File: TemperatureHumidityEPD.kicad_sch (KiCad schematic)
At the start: 66 parts, among them J1 Conn_01x02, J2 FTSH-105-01-L-DV-K, J3 Conn_01x08, J4 Conn_01x24, Q1 Si1308EDL, Q2 IRLML6344, SW1 SW_Push, U1 SI7021, U2 MAX32660GTP, U3 MAX20343H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

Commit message: Fix Part Number for 1k resistor
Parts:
- R6, R7: Part Number RCS06030000Z0EC -> RT0603FRE131KL
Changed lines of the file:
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@@
       (effects (font (size 1.27 1.27)) hide)
     )
-    (property "Part Number" "RCS06030000Z0EC" (at 117.475 184.15 0)
-      (effects (font (size 1.27 1.27)) hide)
-    )
-    (property "Description" "resistor, 0, 0.25W, thick film, SMT, 0603 (1608)" (at 117.475 184.15 0)
+    (property "Part Number" "RT0603FRE131KL" (at 117.475 184.15 0)
+      (effects (font (size 1.27 1.27)) hide)
+    )
+    (property "Description" "resistor, 1k, 0.1W, thin film, 1%, 50ppm, SMT, 0603 (1608)" (at 117.475 184.15 0)
       (effects (font (size 1.27 1.27)) hide)
     )
@@
       (effects (font (size 1.27 1.27)) hide)
     )
-    (property "Part Number" "RCS06030000Z0EC" (at 117.475 179.705 0)
-      (effects (font (size 1.27 1.27)) hide)
-    )
-    (property "Description" "resistor, 0, 0.25W, thick film, SMT, 0603 (1608)" (at 117.475 179.705 0)
-      (effects (font (size 1.27 1.27)) hide)
-    )
+    (property "Part Number" "RT0603FRE131KL" (at 117.475 179.705 0)
+      (effects (font (size 1.27 1.27)) hide)
+    )
+    (property "Description" "resistor, 1k, 0.1W, thin film, 1%, 50ppm, SMT, 0603 (1608)" (at 117.475 179.705 0)
+      (effects (font (size 1.27 1.27)) hide)
+    )

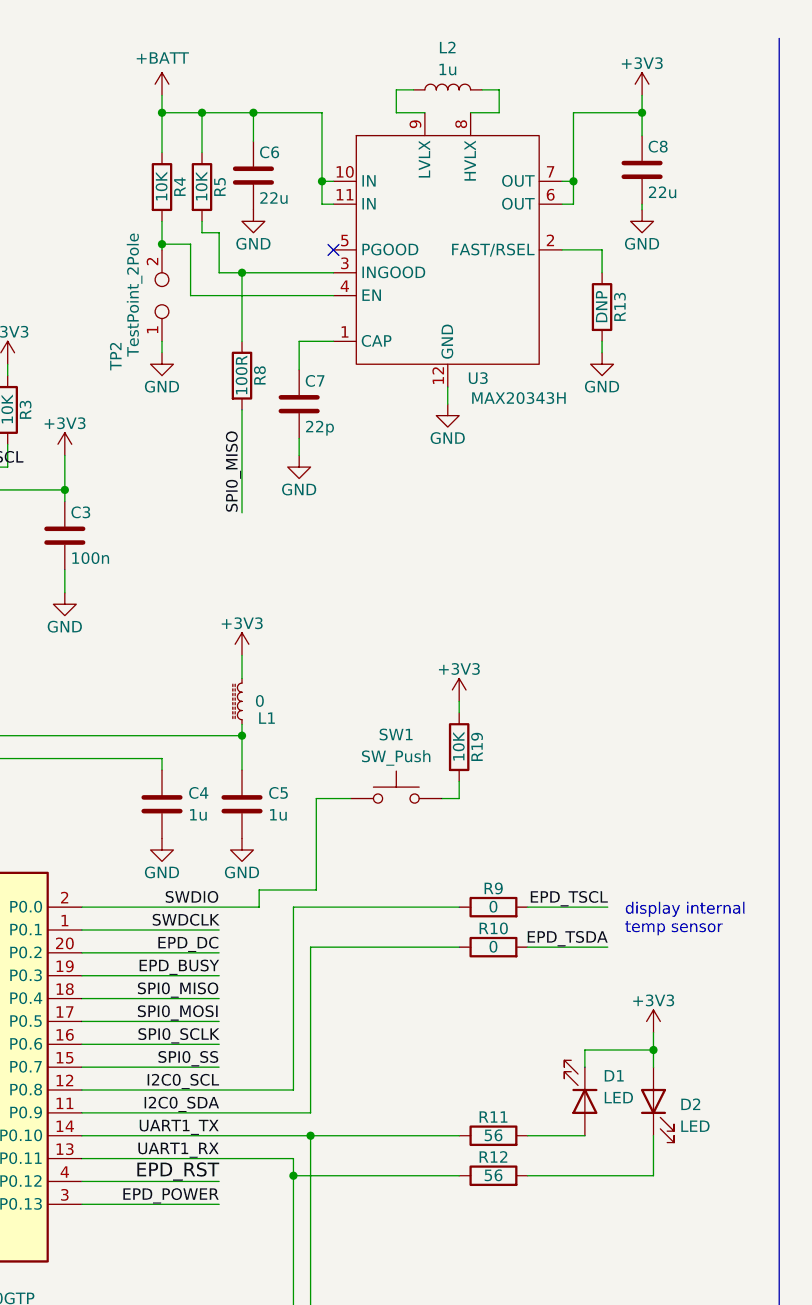
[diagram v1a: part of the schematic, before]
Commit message: Reversed D1 polarity in schematic and PCB. Moved INGOOD pull-up to 3V3 from input net +BATT. Update version and date.
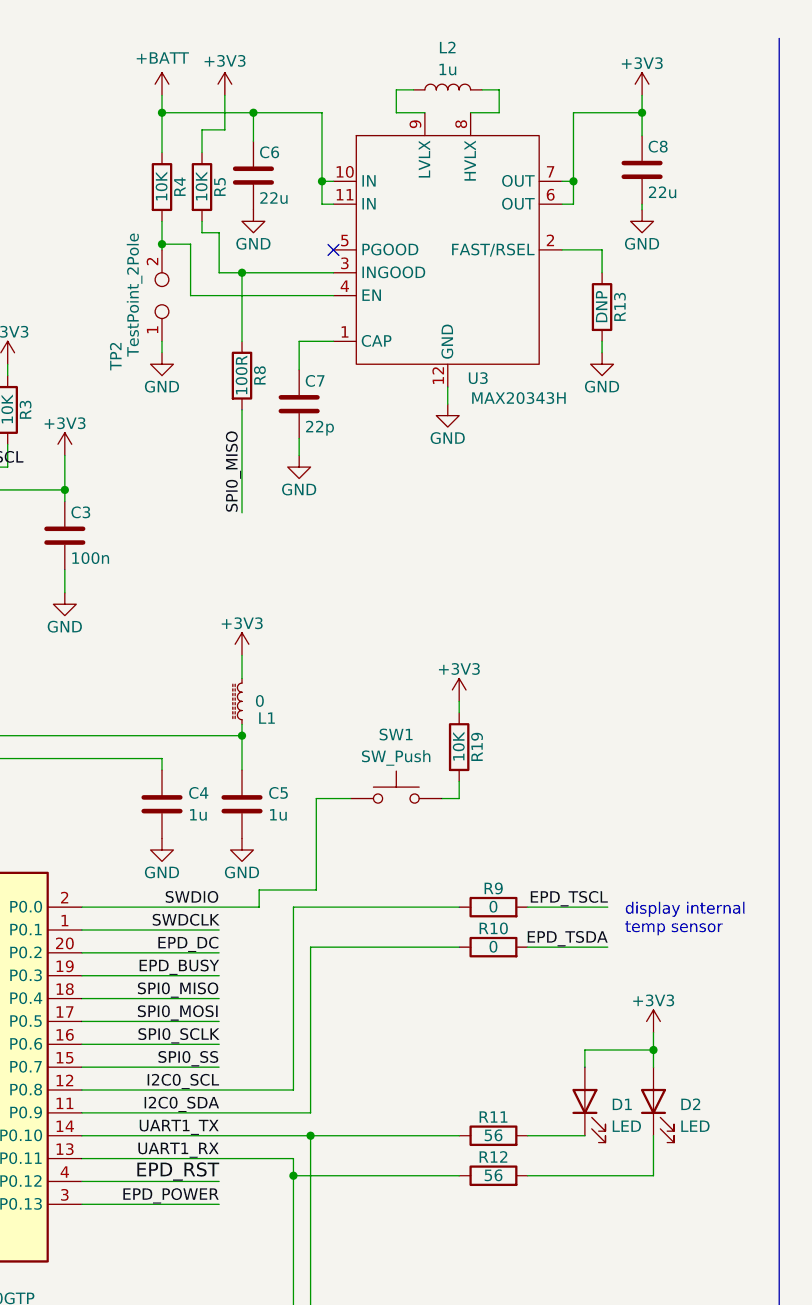
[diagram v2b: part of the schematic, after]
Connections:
- net +3V3: now also D1.2 (A), R5.1; no longer D1.1 (K)
- net +BATT: no longer R5.1
- net at R11.2: now also D1.1 (K); no longer D1.2 (A)
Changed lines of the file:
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@@
   (title_block
     (date "2023-11-30")
+    (rev "0.1-20240304")
   )
   (junction (at 210.82 94.615) (diameter 0) (color 0 0 0 0)
@@
   (junction (at 222.885 94.615) (diameter 0) (color 0 0 0 0)
   )
-  (junction (at 113.665 24.765) (diameter 0) (color 0 0 0 0)
-  )
   (junction (at 211.455 72.39) (diameter 0) (color 0 0 0 0)
   )
@@
     (stroke (width 0) (type default))
   )
-  (wire (pts (xy 113.665 24.765) (xy 119.38 24.765))
+  (wire (pts (xy 109.22 24.765) (xy 119.38 24.765))
     (stroke (width 0) (type default))
   )
@@
     (stroke (width 0) (type default))
   )
+  (wire (pts (xy 116.205 26.67) (xy 113.665 26.67))
+    (stroke (width 0) (type default))
+  )
   (wire (pts (xy 142.24 100.965) (xy 140.335 100.965))
     (stroke (width 0) (type default))
@@
     (stroke (width 0) (type default))
   )
-  (wire (pts (xy 113.665 24.765) (xy 113.665 29.21))
-    (stroke (width 0) (type default))
-  )
   (wire (pts (xy 163.83 128.905) (xy 156.21 128.905))
     (stroke (width 0) (type default))
@@
     (stroke (width 0) (type default))
   )
+  (wire (pts (xy 116.205 22.86) (xy 116.205 26.67))
+    (stroke (width 0) (type default))
+  )
   (wire (pts (xy 153.67 32.385) (xy 154.94 32.385))
     (stroke (width 0) (type default))
@@
     (stroke (width 0) (type default))
   )
+  (wire (pts (xy 113.665 26.67) (xy 113.665 29.21))
+    (stroke (width 0) (type default))
+  )
   (wire (pts (xy 92.075 64.135) (xy 92.075 61.595))
     (stroke (width 0) (type default))
@@
     (stroke (width 0) (type default))
   )
-  (wire (pts (xy 109.22 24.765) (xy 113.665 24.765))
-    (stroke (width 0) (type default))
-  )
   (wire (pts (xy 228.6 137.795) (xy 271.78 137.795))
     (stroke (width 0) (type default))
@@
     )
   )
+  (symbol (lib_id "Device:LED") (at 156.21 134.62 90) (unit 1)
+    (in_bom yes) (on_board yes) (dnp no) (fields_autoplaced)
+    (property "Reference" "D1" (at 159.131 134.9954 90)
+      (effects (font (size 1.27 1.27)) (justify right))
+    )
+    (property "Value" "LED" (at 159.131 137.4196 90)
+      (effects (font (size 1.27 1.27)) (justify right))
+    )
+    (property "Footprint" "LED_SMD:LED_0805_2012Metric_Pad1.15x1.40mm_HandSolder" (at 156.21 134.62 0)
+      (effects (font (size 1.27 1.27)) hide)
+    )
+    (property "Datasheet" "https://www.mouser.com/datasheet/2/180/IN_S85AT_Series_V1_1-2323391.pdf" (at 156.21 134.62 0)
+      (effects (font (size 1.27 1.27)) hide)
+    )
+    (property "Description" "LED, white, SMT, 0805 (2012)" (at 156.21 134.62 0)
+      (effects (font (size 1.27 1.27)) hide)
+    )
+    (property "Part Number" "IN-S85AT5UW" (at 156.21 134.62 0)
+      (effects (font (size 1.27 1.27)) hide)
+    )
+    (pin "1")
+    (pin "2")
+    (instances
+      (project "TemperatureHumidityEPD"
+        (path "/81d518cc-cb14-4db2-89d6-708f10220fa4"
+          (reference "D1") (unit 1)
+        )
+      )
+    )
+  )
   (symbol (lib_id "TemperatureHumidityEPD-rescue:R") (at 146.05 117.475 90) (unit 1)
     (in_bom yes) (on_board yes) (dnp no)
@@
     )
   )
-  (symbol (lib_id "Device:LED") (at 156.21 134.62 270) (unit 1)
-    (in_bom yes) (on_board yes) (dnp no) (fields_autoplaced)
-    (property "Reference" "D1" (at 158.242 131.8204 90)
-      (effects (font (size 1.27 1.27)) (justify left))
-    )
-    (property "Value" "LED" (at 158.242 134.2446 90)
-      (effects (font (size 1.27 1.27)) (justify left))
-    )
-    (property "Footprint" "LED_SMD:LED_0805_2012Metric_Pad1.15x1.40mm_HandSolder" (at 156.21 134.62 0)
-      (effects (font (size 1.27 1.27)) hide)
-    )
-    (property "Datasheet" "https://www.mouser.com/datasheet/2/180/IN_S85AT_Series_V1_1-2323391.pdf" (at 156.21 134.62 0)
-      (effects (font (size 1.27 1.27)) hide)
-    )
-    (property "Description" "LED, white, SMT, 0805 (2012)" (at 156.21 134.62 0)
-      (effects (font (size 1.27 1.27)) hide)
-    )
-    (property "Part Number" "IN-S85AT5UW" (at 156.21 134.62 0)
-      (effects (font (size 1.27 1.27)) hide)
-    )
-    (pin "1")
-    (pin "2")
-    (instances
-      (project "TemperatureHumidityEPD"
-        (path "/81d518cc-cb14-4db2-89d6-708f10220fa4"
-          (reference "D1") (unit 1)
-        )
-      )
-    )
-  )
   (symbol (lib_id "TemperatureHumidityEPD-rescue:+3V3") (at 163.83 127 0) (unit 1)
     (in_bom yes) (on_board yes) (dnp no)
@@
         )
       )
+    )
+  )
+  (symbol (lib_id "TemperatureHumidityEPD-rescue:+3V3") (at 116.205 22.86 0) (unit 1)
+    (in_bom yes) (on_board yes) (dnp no)
+    (property "Reference" "#PWR046" (at 116.205 26.67 0)
+      (effects (font (size 1.27 1.27)) hide)
+    )
+    (property "Value" "+3V3" (at 116.205 19.05 0)
+      (effects (font (size 1.27 1.27)))
+    )
+    (property "Footprint" "" (at 116.205 22.86 0)
+      (effects (font (size 1.27 1.27)) hide)
+    )
+    (property "Datasheet" "" (at 116.205 22.86 0)
+      (effects (font (size 1.27 1.27)) hide)
+    )
+    (pin "1")
+    (instances
+      (project "TemperatureHumidityEPD"
+        (path "/81d518cc-cb14-4db2-89d6-708f10220fa4"
+          (reference "#PWR046") (unit 1)
+        )
+      )
